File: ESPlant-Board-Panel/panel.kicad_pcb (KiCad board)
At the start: 4 copper layers, 142 x 116 mm, 342 parts, among them J1 Conn_01x05, U1 HC-TYPE-C-16P-01A-G, U13 ESP32-C6-MINI-1/U, U3 AHT20-F, U5 TPS61025DRCR, U6 Light sensor, U7 TS-1088-AR02016, U8 MK-12C02-G025

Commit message: Panel: Update production files
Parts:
- removed the BZ1 at (173.0, 57.5)
- removed the BZ1 at (251.0, 57.5)
- removed the BZ1 at (277.0, 57.5)
- removed the BZ1 at (199.0, 57.5)
- removed the BZ1 at (225.0, 57.5)
- removed the C1 at (220.5, 44.9)
- removed the C1 at (246.5, 44.9)
- removed the C1 at (194.5, 44.9)
- removed the C1 at (272.5, 44.9)
- removed the C1 at (168.5, 44.9)
- removed the C10 at (272.5, 51.2)
- removed the C10 at (194.5, 51.2)
- removed the C10 at (220.5, 51.2)
- removed the C10 at (246.5, 51.2)
- removed the C10 at (168.5, 51.2)
- removed the C2 at (168.5, 42.8)
- removed the C2 at (194.5, 42.8)
- removed the C2 at (272.5, 42.8)
- removed the C2 at (220.5, 42.8)
- removed the C2 at (246.5, 42.8)
- removed the C3 at (243.5, 32.2)
- removed the C3 at (191.5, 32.2)
- removed the C3 at (217.5, 32.2)
- removed the C3 at (165.5, 32.2)
- removed the C3 at (269.5, 32.2)
- removed the C4 at (199.0, 81.0)
- removed the C4 at (277.0, 81.0)
- removed the C4 at (173.0, 81.0)
- removed the C4 at (225.0, 81.0)
- removed the C4 at (251.0, 81.0)
- removed the C6 at (194.5, 49.7)
- removed the C6 at (246.5, 49.7)
- removed the C6 at (168.5, 49.7)
- removed the C6 at (272.5, 49.7)
- removed the C6 at (220.5, 49.7)
- removed the C7 at (255.3, 33.3)
- removed the C7 at (281.3, 33.3)
- removed the C7 at (229.3, 33.3)
- removed the C7 at (203.3, 33.3)
- removed the C7 at (177.3, 33.3)
- removed the C8 at (189.5, 22.4)
- removed the C8 at (215.5, 22.4)
- removed the C8 at (241.5, 22.4)
- removed the C8 at (267.5, 22.4)
- removed the C8 at (163.5, 22.4)
- removed the C9 at (240.5, 22.4)
- removed the C9 at (266.5, 22.4)
- removed the C9 at (162.5, 22.4)
- removed the C9 at (214.5, 22.4)
- removed the C9 at (188.5, 22.4)
- removed the D1 at (260.5, 35.3)
- removed the D1 at (208.5, 35.3)
- removed the D1 at (182.5, 35.3)
- removed the D1 at (286.5, 35.3)
- removed the D1 at (234.5, 35.3)
- removed the D2 at (219.3, 34.8)
- removed the D2 at (245.3, 34.8)
- removed the D2 at (193.3, 34.8)
- removed the D2 at (271.3, 34.8)
- removed the D2 at (167.3, 34.8)
- removed the D3 at (260.5, 33.0)
- removed the D3 at (286.5, 33.0)
- removed the D3 at (182.5, 33.0)
- removed the D3 at (234.5, 33.0)
- removed the D3 at (208.5, 33.0)
- removed the H1 at (286.4, 22.6)
- removed the H1 at (182.4, 22.6)
- removed the H1 at (260.4, 22.6)
- removed the H1 at (234.4, 22.6)
- removed the H1 at (208.4, 22.6)
- removed the H2 at (191.0, 60.0)
- removed the H2 at (243.0, 60.0)
- removed the H2 at (269.0, 60.0)
- removed the H2 at (165.0, 60.0)
- removed the H2 at (217.0, 60.0)
- removed the H3 at (259.0, 60.0)
- removed the H3 at (233.0, 60.0)
- removed the H3 at (285.0, 60.0)
- removed the H3 at (207.0, 60.0)
- removed the H3 at (181.0, 60.0)
- removed the J1 at (239.9, 42.4)
- removed the J1 at (187.9, 42.4)
- removed the J1 at (213.9, 42.4)
- removed the J1 at (265.9, 42.4)
- removed the J1 at (161.9, 42.4)
- removed the L1 at (198.5, 47.6)
- removed the L1 at (172.5, 47.6)
- removed the L1 at (250.5, 47.6)
- removed the L1 at (276.5, 47.6)
- removed the L1 at (224.5, 47.6)
- removed the R1 at (190.3, 45.3)
- removed the R1 at (164.3, 45.3)
- removed the R1 at (242.3, 45.3)
- removed the R1 at (216.3, 45.3)
- removed the R1 at (268.3, 45.3)
- removed the R10 at (283.4, 27.8)
- removed the R10 at (179.4, 27.8)
- removed the R10 at (231.4, 27.8)
- removed the R10 at (257.4, 27.8)
- removed the R10 at (205.4, 27.8)
- removed the R11 at (253.7, 43.0)
- removed the R11 at (175.7, 43.0)
- removed the R11 at (279.7, 43.0)
- removed the R11 at (227.7, 43.0)
- removed the R11 at (201.7, 43.0)
- removed the R12 at (253.7, 40.1)
- removed the R12 at (279.7, 40.1)
- removed the R12 at (175.7, 40.1)
- removed the R12 at (201.7, 40.1)
- removed the R12 at (227.7, 40.1)
- removed the R13 at (205.9, 35.3)
- removed the R13 at (231.9, 35.3)
- removed the R13 at (179.9, 35.3)
- removed the R13 at (257.9, 35.3)
- removed the R13 at (283.9, 35.3)
- removed the R14 at (179.9, 33.4)
- removed the R14 at (205.9, 33.4)
- removed the R14 at (231.9, 33.4)
- removed the R14 at (283.9, 33.4)
- removed the R14 at (257.9, 33.4)
- removed the R15 at (164.3, 46.3)
- removed the R15 at (216.3, 46.3)
- removed the R15 at (268.3, 46.3)
- removed the R15 at (242.3, 46.3)
- removed the R15 at (190.3, 46.3)
- removed the R16 at (190.8, 47.8)
- removed the R16 at (268.8, 47.8)
- removed the R16 at (216.8, 47.8)
- removed the R16 at (242.8, 47.8)
- removed the R16 at (164.8, 47.8)
- removed the R2 at (179.4, 25.9)
- removed the R2 at (283.4, 25.9)
- removed the R2 at (257.4, 25.9)
- removed the R2 at (205.4, 25.9)
- removed the R2 at (231.4, 25.9)
- removed the R3 at (203.3, 34.3)
- removed the R3 at (177.3, 34.3)
- removed the R3 at (229.3, 34.3)
- removed the R3 at (255.3, 34.3)
- removed the R3 at (281.3, 34.3)
- removed the R4 at (243.8, 37.9)
- removed the R4 at (165.8, 37.9)
- removed the R4 at (217.8, 37.9)
- removed the R4 at (191.8, 37.9)
- removed the R4 at (269.8, 37.9)
- removed the R5 at (173.6, 32.4)
- removed the R5 at (199.6, 32.4)
- removed the R5 at (251.6, 32.4)
- removed the R5 at (277.6, 32.4)
- removed the R5 at (225.6, 32.4)
- removed the R6 at (167.0, 36.9)
- removed the R6 at (193.0, 36.9)
- removed the R6 at (219.0, 36.9)
- removed the R6 at (245.0, 36.9)
- removed the R6 at (271.0, 36.9)
- removed the R7 at (227.1, 37.8)
- removed the R7 at (201.1, 37.8)
- removed the R7 at (175.1, 37.8)
- removed the R7 at (253.1, 37.8)
- removed the R7 at (279.1, 37.8)
- removed the R8 at (273.4, 32.6)
- removed the R8 at (195.4, 32.6)
- removed the R8 at (221.4, 32.6)
- removed the R8 at (247.4, 32.6)
- removed the R8 at (169.4, 32.6)
- removed the R9 at (215.0, 27.1)
- removed the R9 at (163.0, 27.1)
- removed the R9 at (267.0, 27.1)
- removed the R9 at (241.0, 27.1)
- removed the R9 at (189.0, 27.1)
- removed the U1 at (180.0, 41.6)
- removed the U1 at (232.0, 41.6)
- removed the U1 at (284.0, 41.6)
- removed the U1 at (206.0, 41.6)
- removed the U1 at (258.0, 41.6)
- removed the U13 at (274.9, 25.5)
- removed the U13 at (248.9, 25.5)
- removed the U13 at (196.9, 25.5)
- removed the U13 at (222.9, 25.5)
- removed the U13 at (170.9, 25.5)
- removed the U3 at (182.0, 28.1)
- removed the U3 at (208.0, 28.1)
- removed the U3 at (286.0, 28.1)
- removed the U3 at (234.0, 28.1)
- removed the U3 at (260.0, 28.1)
- removed the U5 at (246.5, 47.3)
- removed the U5 at (168.5, 47.3)
- removed the U5 at (272.5, 47.3)
- removed the U5 at (220.5, 47.3)
- removed the U5 at (194.5, 47.3)
- removed the U6 at (182.0, 30.9)
- removed the U6 at (234.0, 30.9)
- removed the U6 at (208.0, 30.9)
- removed the U6 at (260.0, 30.9)
- removed the U6 at (286.0, 30.9)
- removed the U7 at (242.7, 54.5)
- removed the U7 at (268.7, 54.5)
- removed the U7 at (164.7, 54.5)
- removed the U7 at (190.7, 54.5)
- removed the U7 at (216.7, 54.5)
- removed the U8 at (234.6, 51.5)
- removed the U8 at (286.6, 51.5)
- removed the U8 at (208.6, 51.5)
- removed the U8 at (182.6, 51.5)
- removed the U8 at (260.6, 51.5)
- removed the U9 at (277.0, 64.5)
- removed the U9 at (251.0, 64.5)
- removed the U9 at (173.0, 64.5)
- removed the U9 at (225.0, 64.5)
- removed the U9 at (199.0, 64.5)
- added BZ1: Buzzer, CustomFootprints:BUZ-SMD_4P-L8.5-W8.5-P8.50-BR, F.Cu at (173.0, 57.9)
- added BZ1: Buzzer, CustomFootprints:BUZ-SMD_4P-L8.5-W8.5-P8.50-BR, F.Cu at (277.0, 57.9)
- added BZ1: Buzzer, CustomFootprints:BUZ-SMD_4P-L8.5-W8.5-P8.50-BR, F.Cu at (199.0, 57.9)
- added BZ1: Buzzer, CustomFootprints:BUZ-SMD_4P-L8.5-W8.5-P8.50-BR, F.Cu at (225.0, 57.9)
- added BZ1: Buzzer, CustomFootprints:BUZ-SMD_4P-L8.5-W8.5-P8.50-BR, F.Cu at (251.0, 57.9)
- added C1: 2.2uF-Ceramic, Capacitor_SMD:C_0402_1005Metric, F.Cu at (258.3, 37.7)
- added C1: 2.2uF-Ceramic, Capacitor_SMD:C_0402_1005Metric, F.Cu at (180.3, 37.7)
- added C1: 2.2uF-Ceramic, Capacitor_SMD:C_0402_1005Metric, F.Cu at (284.3, 37.7)
- added C1: 2.2uF-Ceramic, Capacitor_SMD:C_0402_1005Metric, F.Cu at (206.3, 37.7)
- added C1: 2.2uF-Ceramic, Capacitor_SMD:C_0402_1005Metric, F.Cu at (232.3, 37.7)
- added C10: 10uF-Tantalum, CustomFootprints:CAP-SMD_L3.2-W1.6-RD-C7171, F.Cu at (200.0, 37.7)
- added C10: 10uF-Tantalum, CustomFootprints:CAP-SMD_L3.2-W1.6-RD-C7171, F.Cu at (278.0, 37.7)
- added C10: 10uF-Tantalum, CustomFootprints:CAP-SMD_L3.2-W1.6-RD-C7171, F.Cu at (252.0, 37.7)
- added C10: 10uF-Tantalum, CustomFootprints:CAP-SMD_L3.2-W1.6-RD-C7171, F.Cu at (226.0, 37.7)
- added C10: 10uF-Tantalum, CustomFootprints:CAP-SMD_L3.2-W1.6-RD-C7171, F.Cu at (174.0, 37.7)
- added C2: 100uF-Tantalum, CustomFootprints:CASE-B_3528, F.Cu at (234.4, 37.7)
- added C2: 100uF-Tantalum, CustomFootprints:CASE-B_3528, F.Cu at (208.4, 37.7)
- added C2: 100uF-Tantalum, CustomFootprints:CASE-B_3528, F.Cu at (182.4, 37.7)
- added C2: 100uF-Tantalum, CustomFootprints:CASE-B_3528, F.Cu at (260.4, 37.7)
- added C2: 100uF-Tantalum, CustomFootprints:CASE-B_3528, F.Cu at (286.4, 37.7)
- added C3: 10nF, Capacitor_SMD:C_0402_1005Metric, F.Cu at (219.1, 33.1)
- added C3: 10nF, Capacitor_SMD:C_0402_1005Metric, F.Cu at (271.1, 33.1)
- added C3: 10nF, Capacitor_SMD:C_0402_1005Metric, F.Cu at (167.1, 33.1)
- added C3: 10nF, Capacitor_SMD:C_0402_1005Metric, F.Cu at (245.1, 33.1)
- added C3: 10nF, Capacitor_SMD:C_0402_1005Metric, F.Cu at (193.1, 33.1)
- added C4: 7pF-27pF, A=2.75cm^2, CustomFootprints:Sensor-Tip, B.Cu at (251.0, 81.0)
- added C4: 7pF-27pF, A=2.75cm^2, CustomFootprints:Sensor-Tip, B.Cu at (173.0, 81.0)
- added C4: 7pF-27pF, A=2.75cm^2, CustomFootprints:Sensor-Tip, B.Cu at (277.0, 81.0)
- added C4: 7pF-27pF, A=2.75cm^2, CustomFootprints:Sensor-Tip, B.Cu at (199.0, 81.0)
- added C4: 7pF-27pF, A=2.75cm^2, CustomFootprints:Sensor-Tip, B.Cu at (225.0, 81.0)
- added C6: 100nF-Ceramic, Capacitor_SMD:C_0402_1005Metric, F.Cu at (253.5, 37.7)
- added C6: 100nF-Ceramic, Capacitor_SMD:C_0402_1005Metric, F.Cu at (279.5, 37.7)
- added C6: 100nF-Ceramic, Capacitor_SMD:C_0402_1005Metric, F.Cu at (201.5, 37.7)
- added C6: 100nF-Ceramic, Capacitor_SMD:C_0402_1005Metric, F.Cu at (175.5, 37.7)
- added C6: 100nF-Ceramic, Capacitor_SMD:C_0402_1005Metric, F.Cu at (227.5, 37.7)
- added C7: 10uF, Capacitor_SMD:C_0402_1005Metric, F.Cu at (163.5, 26.9)
- added C7: 10uF, Capacitor_SMD:C_0402_1005Metric, F.Cu at (241.5, 26.9)
- added C7: 10uF, Capacitor_SMD:C_0402_1005Metric, F.Cu at (189.5, 26.9)
- added C7: 10uF, Capacitor_SMD:C_0402_1005Metric, F.Cu at (215.5, 26.9)
- added C7: 10uF, Capacitor_SMD:C_0402_1005Metric, F.Cu at (267.5, 26.9)
- added C8: 10nF, Capacitor_SMD:C_0402_1005Metric, F.Cu at (242.8, 22.4)
- added C8: 10nF, Capacitor_SMD:C_0402_1005Metric, F.Cu at (164.8, 22.4)
- added C8: 10nF, Capacitor_SMD:C_0402_1005Metric, F.Cu at (190.8, 22.4)
- added C8: 10nF, Capacitor_SMD:C_0402_1005Metric, F.Cu at (216.8, 22.4)
- added C8: 10nF, Capacitor_SMD:C_0402_1005Metric, F.Cu at (268.8, 22.4)
- added C9: 10uF, Capacitor_SMD:C_0402_1005Metric, F.Cu at (215.8, 22.4)
- added C9: 10uF, Capacitor_SMD:C_0402_1005Metric, F.Cu at (267.8, 22.4)
- added C9: 10uF, Capacitor_SMD:C_0402_1005Metric, F.Cu at (241.8, 22.4)
- added C9: 10uF, Capacitor_SMD:C_0402_1005Metric, F.Cu at (163.8, 22.4)
- added C9: 10uF, Capacitor_SMD:C_0402_1005Metric, F.Cu at (189.8, 22.4)
- added D1: GREEN, CustomFootprints:LED0805-R-RD, F.Cu at (269.7, 40.5)
- added D1: GREEN, CustomFootprints:LED0805-R-RD, F.Cu at (191.7, 40.5)
- added D1: GREEN, CustomFootprints:LED0805-R-RD, F.Cu at (217.7, 40.5)
- added D1: GREEN, CustomFootprints:LED0805-R-RD, F.Cu at (243.7, 40.5)
- added D1: GREEN, CustomFootprints:LED0805-R-RD, F.Cu at (165.7, 40.5)
- added D2: Switching-Diode, CustomFootprints:SOD-123F_L2.7-W1.6-LS3.8-RD, F.Cu at (194.8, 34.7)
- added D2: Switching-Diode, CustomFootprints:SOD-123F_L2.7-W1.6-LS3.8-RD, F.Cu at (246.8, 34.7)
- added D2: Switching-Diode, CustomFootprints:SOD-123F_L2.7-W1.6-LS3.8-RD, F.Cu at (168.8, 34.7)
- added D2: Switching-Diode, CustomFootprints:SOD-123F_L2.7-W1.6-LS3.8-RD, F.Cu at (272.8, 34.7)
- added D2: Switching-Diode, CustomFootprints:SOD-123F_L2.7-W1.6-LS3.8-RD, F.Cu at (220.8, 34.7)
- added D3: RED, CustomFootprints:LED0805-R-RD, F.Cu at (241.7, 40.5)
- added D3: RED, CustomFootprints:LED0805-R-RD, F.Cu at (189.7, 40.5)
- added D3: RED, CustomFootprints:LED0805-R-RD, F.Cu at (215.7, 40.5)
- added D3: RED, CustomFootprints:LED0805-R-RD, F.Cu at (267.7, 40.5)
- added D3: RED, CustomFootprints:LED0805-R-RD, F.Cu at (163.7, 40.5)
- added H1: MountingHole, MountingHole:MountingHole_3.2mm_M3, F.Cu at (234.4, 22.6)
- added H1: MountingHole, MountingHole:MountingHole_3.2mm_M3, F.Cu at (286.4, 22.6)
- added H1: MountingHole, MountingHole:MountingHole_3.2mm_M3, F.Cu at (260.4, 22.6)
- added H1: MountingHole, MountingHole:MountingHole_3.2mm_M3, F.Cu at (208.4, 22.6)
- added H1: MountingHole, MountingHole:MountingHole_3.2mm_M3, F.Cu at (182.4, 22.6)
- added H2: MountingHole, MountingHole:MountingHole_3.2mm_M3, F.Cu at (241.6, 60.7)
- added H2: MountingHole, MountingHole:MountingHole_3.2mm_M3, F.Cu at (267.6, 60.7)
- added H2: MountingHole, MountingHole:MountingHole_3.2mm_M3, F.Cu at (189.6, 60.7)
- added H2: MountingHole, MountingHole:MountingHole_3.2mm_M3, F.Cu at (215.6, 60.7)
- added H2: MountingHole, MountingHole:MountingHole_3.2mm_M3, F.Cu at (163.6, 60.7)
- added H3: MountingHole, MountingHole:MountingHole_3.2mm_M3, F.Cu at (234.4, 60.7)
- added H3: MountingHole, MountingHole:MountingHole_3.2mm_M3, F.Cu at (182.4, 60.7)
- added H3: MountingHole, MountingHole:MountingHole_3.2mm_M3, F.Cu at (208.4, 60.7)
- added H3: MountingHole, MountingHole:MountingHole_3.2mm_M3, F.Cu at (260.4, 60.7)
- added H3: MountingHole, MountingHole:MountingHole_3.2mm_M3, F.Cu at (286.4, 60.7)
- added J1: Conn_01x05, CustomFootprints:PinHeader_1x05_P2.54mm_Vertical_SMD, B.Cu at (240.0, 35.8)
- added J1: Conn_01x05, CustomFootprints:PinHeader_1x05_P2.54mm_Vertical_SMD, B.Cu at (188.0, 35.8)
- added J1: Conn_01x05, CustomFootprints:PinHeader_1x05_P2.54mm_Vertical_SMD, B.Cu at (162.0, 35.8)
- added J1: Conn_01x05, CustomFootprints:PinHeader_1x05_P2.54mm_Vertical_SMD, B.Cu at (266.0, 35.8)
- added J1: Conn_01x05, CustomFootprints:PinHeader_1x05_P2.54mm_Vertical_SMD, B.Cu at (214.0, 35.8)
- added L1: 6.8uH, CustomFootprints:IND-SMD_L3.5-W3.0, F.Cu at (281.6, 41.7)
- added L1: 6.8uH, CustomFootprints:IND-SMD_L3.5-W3.0, F.Cu at (255.6, 41.7)
- added L1: 6.8uH, CustomFootprints:IND-SMD_L3.5-W3.0, F.Cu at (177.6, 41.7)
- added L1: 6.8uH, CustomFootprints:IND-SMD_L3.5-W3.0, F.Cu at (229.6, 41.7)
- added L1: 6.8uH, CustomFootprints:IND-SMD_L3.5-W3.0, F.Cu at (203.6, 41.7)
- added R1: 100k, Resistor_SMD:R_0402_1005Metric, F.Cu at (205.9, 33.5)
- added R1: 100k, Resistor_SMD:R_0402_1005Metric, F.Cu at (257.9, 33.5)
- added R1: 100k, Resistor_SMD:R_0402_1005Metric, F.Cu at (179.9, 33.5)
- added R1: 100k, Resistor_SMD:R_0402_1005Metric, F.Cu at (231.9, 33.5)
- added R1: 100k, Resistor_SMD:R_0402_1005Metric, F.Cu at (283.9, 33.5)
- added R10: 5k1, Resistor_SMD:R_0402_1005Metric, F.Cu at (179.4, 27.9)
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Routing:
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- added copper zone on F.Cu, net Board_0-PWR_VIN
- added copper zone on F.Cu, net Board_1-PWR_VIN
- added copper zone on F.Cu, net Board_2-PWR_VIN
- added copper zone on F.Cu, net Board_3-PWR_VIN
- added copper zone on F.Cu, net Board_4-PWR_VIN
- removed copper zone on F.Cu, net Board_0-VCC
- removed copper zone on F.Cu, net Board_1-VCC
- removed copper zone on F.Cu, net Board_2-VCC
- removed copper zone on F.Cu, net Board_3-VCC
- removed copper zone on F.Cu, net Board_4-VCC
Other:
- outline, holes or cut-outs redrawn
- board text added: "Reset"
- board text added: "USB〡BAT"

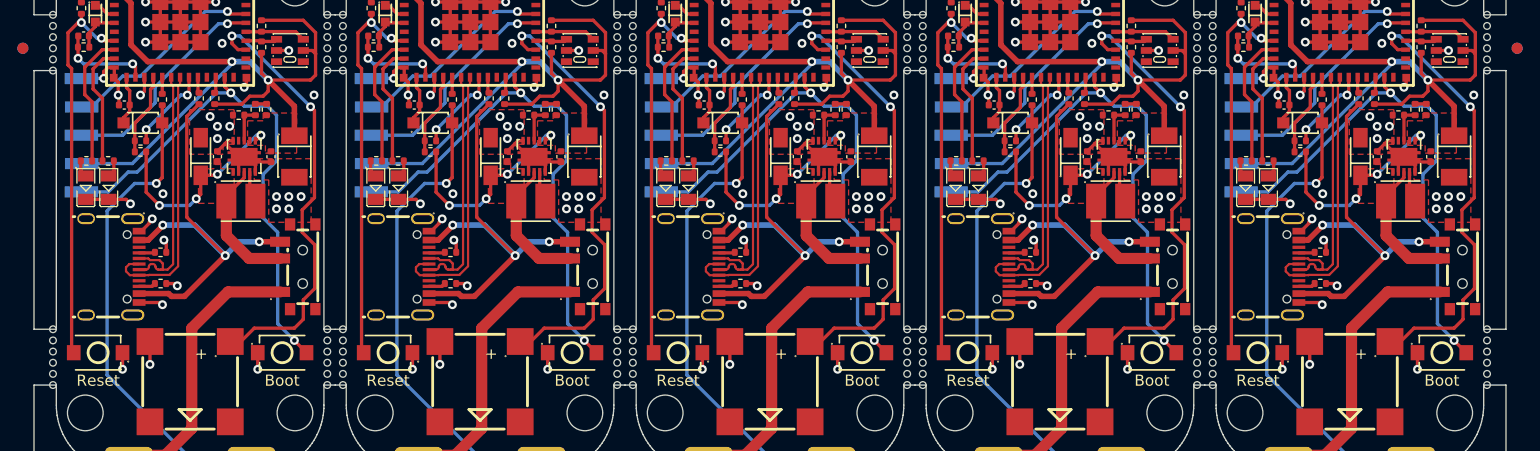
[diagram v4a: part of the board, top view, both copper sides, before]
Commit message: Board: Add debouncing caps to buttons
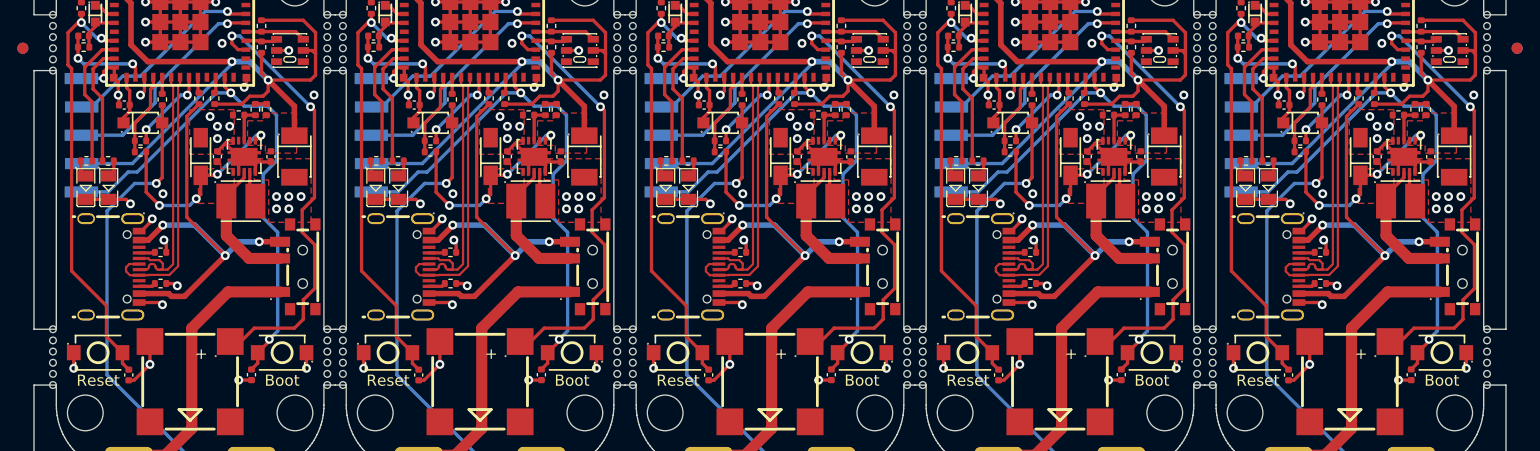
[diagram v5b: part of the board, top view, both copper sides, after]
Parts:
- added C11: 100nF-Ceramic, Capacitor_SMD:C_0402_1005Metric, F.Cu at (219.5, 57.3)
- added C11: 100nF-Ceramic, Capacitor_SMD:C_0402_1005Metric, F.Cu at (245.5, 57.3)
- added C11: 100nF-Ceramic, Capacitor_SMD:C_0402_1005Metric, F.Cu at (167.5, 57.3)
- added C11: 100nF-Ceramic, Capacitor_SMD:C_0402_1005Metric, F.Cu at (193.5, 57.3)
- added C11: 100nF-Ceramic, Capacitor_SMD:C_0402_1005Metric, F.Cu at (271.5, 57.3)
- added C5: 100nF-Ceramic, Capacitor_SMD:C_0402_1005Metric, F.Cu at (256.5, 57.3)
- added C5: 100nF-Ceramic, Capacitor_SMD:C_0402_1005Metric, F.Cu at (230.5, 57.3)
- added C5: 100nF-Ceramic, Capacitor_SMD:C_0402_1005Metric, F.Cu at (282.5, 57.3)
- added C5: 100nF-Ceramic, Capacitor_SMD:C_0402_1005Metric, F.Cu at (204.5, 57.3)
- added C5: 100nF-Ceramic, Capacitor_SMD:C_0402_1005Metric, F.Cu at (178.5, 57.3)
- turned U4 to 0 degrees (x5)
- turned U7 to 180 degrees (x5)
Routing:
- net Board_1-GND: track 214.8 -> 218.5 mm, vias 47 -> 48
- net Board_0-GND: track 214.8 -> 218.5 mm, vias 47 -> 48
- net Board_2-GND: track 214.8 -> 218.5 mm, vias 47 -> 48
- net Board_4-GND: track 214.8 -> 218.5 mm, vias 47 -> 48
- net Board_3-GND: track 214.8 -> 218.5 mm, vias 47 -> 48
- net Board_2-EN: track 34.9 -> 38.5 mm
- net Board_4-EN: track 34.9 -> 38.5 mm
- net Board_3-EN: track 34.9 -> 38.5 mm
- net Board_1-EN: track 34.9 -> 38.5 mm
- net Board_0-EN: track 34.9 -> 38.5 mm
- net Board_3-IO9: track 47.0 -> 48.4 mm
- net Board_4-IO9: track 47.0 -> 48.4 mm
- net Board_2-IO9: track 47.0 -> 48.4 mm
- net Board_0-IO9: track 47.0 -> 48.4 mm
- net Board_1-IO9: track 47.0 -> 48.4 mm

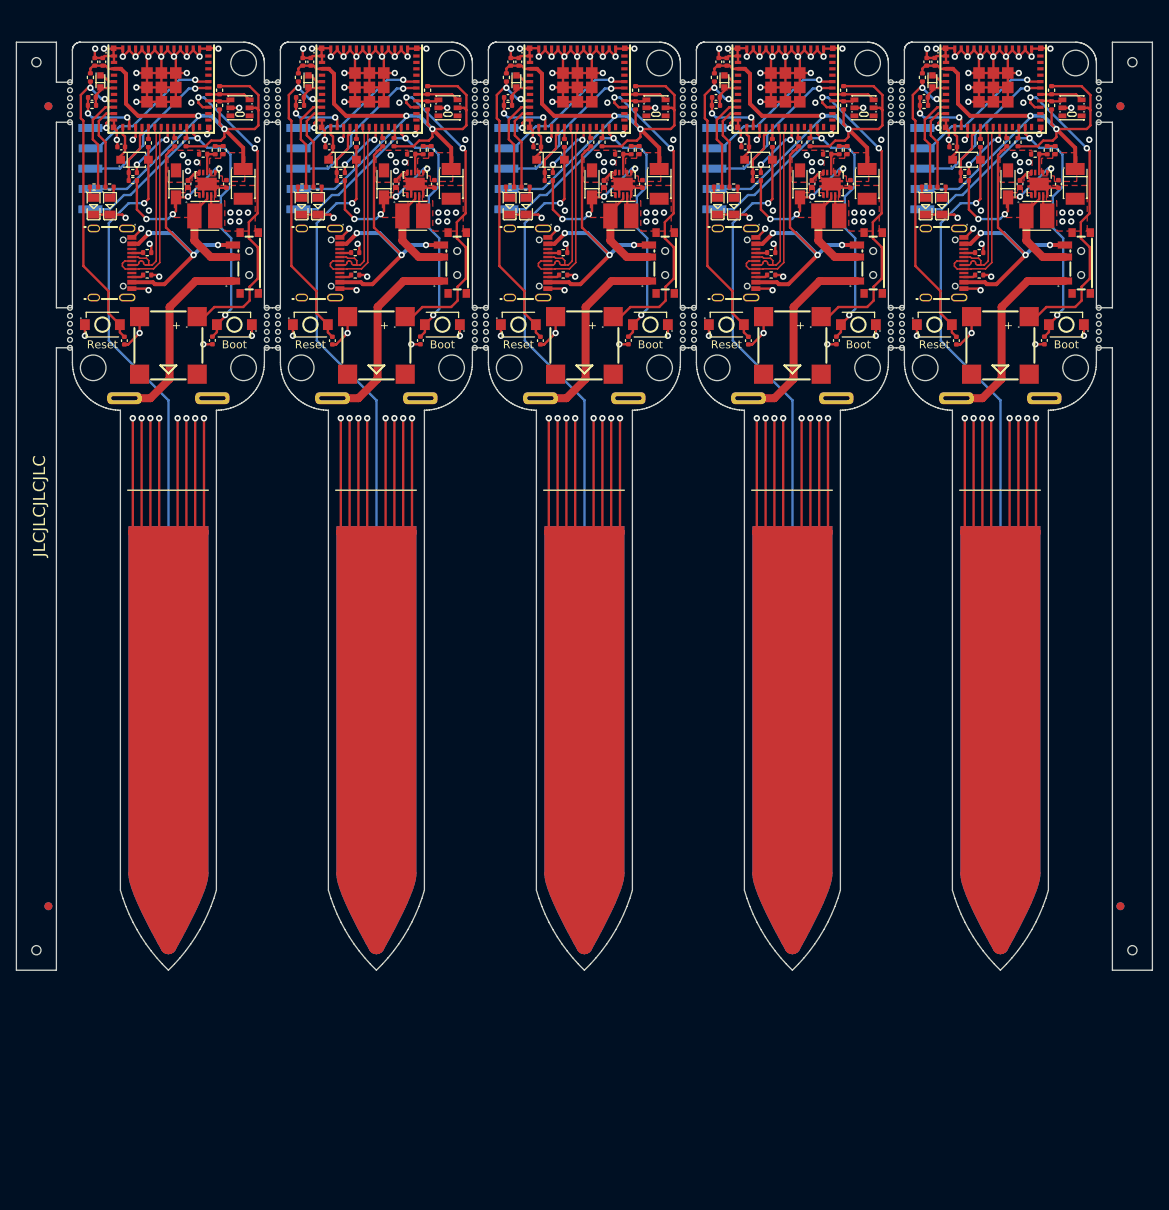
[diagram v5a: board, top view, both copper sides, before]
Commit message: Panel: 2 columns
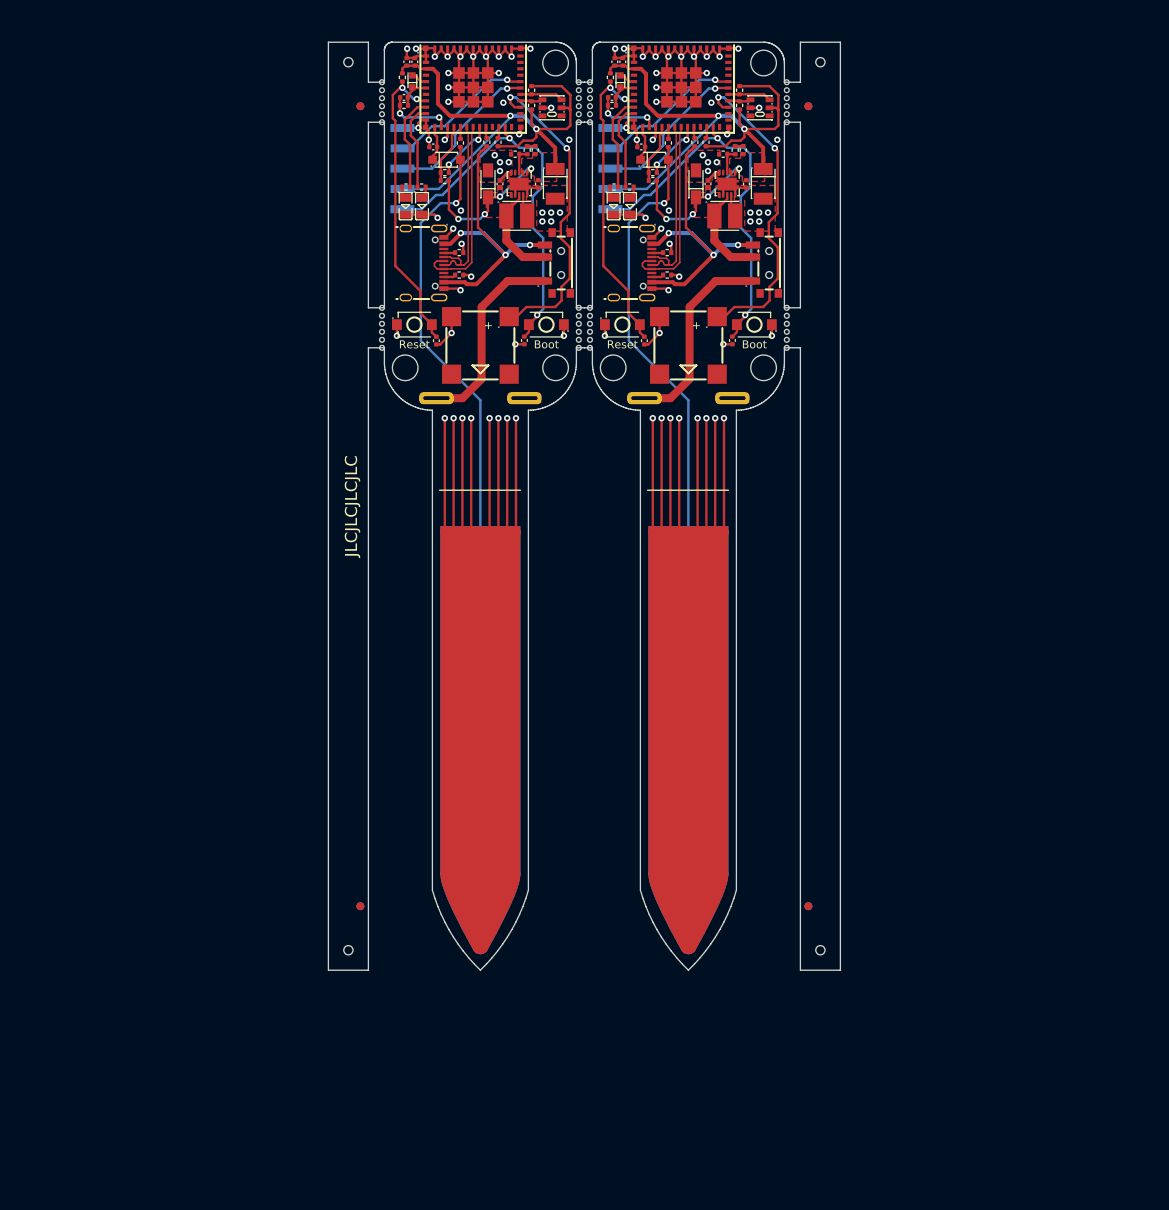
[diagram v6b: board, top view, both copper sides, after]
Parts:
- removed the BZ1 at (199.0, 57.9)
- removed the BZ1 at (251.0, 57.9)
- removed the BZ1 at (277.0, 57.9)
- removed the BZ1 at (225.0, 57.9)
- removed the BZ1 at (173.0, 57.9)
- removed the C1 at (232.3, 37.7)
- removed the C1 at (180.3, 37.7)
- removed the C1 at (258.3, 37.7)
- removed the C1 at (284.3, 37.7)
- removed the C1 at (206.3, 37.7)
- removed the C10 at (252.0, 37.7)
- removed the C10 at (200.0, 37.7)
- removed the C10 at (226.0, 37.7)
- removed the C10 at (278.0, 37.7)
- removed the C10 at (174.0, 37.7)
- removed the C11 at (219.5, 57.3)
- removed the C11 at (245.5, 57.3)
- removed the C11 at (167.5, 57.3)
- removed the C11 at (193.5, 57.3)
- removed the C11 at (271.5, 57.3)
- removed the C2 at (260.4, 37.7)
- removed the C2 at (234.4, 37.7)
- removed the C2 at (182.4, 37.7)
- removed the C2 at (286.4, 37.7)
- removed the C2 at (208.4, 37.7)
- removed the C3 at (245.1, 33.1)
- removed the C3 at (167.1, 33.1)
- removed the C3 at (219.1, 33.1)
- removed the C3 at (271.1, 33.1)
- removed the C3 at (193.1, 33.1)
- removed the C4 at (199.0, 81.0)
- removed the C4 at (277.0, 81.0)
- removed the C4 at (251.0, 81.0)
- removed the C4 at (173.0, 81.0)
- removed the C4 at (225.0, 81.0)
- removed the C5 at (256.5, 57.3)
- removed the C5 at (230.5, 57.3)
- removed the C5 at (282.5, 57.3)
- removed the C5 at (204.5, 57.3)
- removed the C5 at (178.5, 57.3)
- removed the C6 at (279.5, 37.7)
- removed the C6 at (253.5, 37.7)
- removed the C6 at (175.5, 37.7)
- removed the C6 at (201.5, 37.7)
- removed the C6 at (227.5, 37.7)
- removed the C7 at (163.5, 26.9)
- removed the C7 at (241.5, 26.9)
- removed the C7 at (267.5, 26.9)
- removed the C7 at (215.5, 26.9)
- removed the C7 at (189.5, 26.9)
- removed the C8 at (216.8, 22.4)
- removed the C8 at (190.8, 22.4)
- removed the C8 at (242.8, 22.4)
- removed the C8 at (268.8, 22.4)
- removed the C8 at (164.8, 22.4)
- removed the C9 at (241.8, 22.4)
- removed the C9 at (215.8, 22.4)
- removed the C9 at (189.8, 22.4)
- removed the C9 at (267.8, 22.4)
- removed the C9 at (163.8, 22.4)
- removed the D1 at (217.7, 40.5)
- removed the D1 at (243.7, 40.5)
- removed the D1 at (269.7, 40.5)
- removed the D1 at (191.7, 40.5)
- removed the D1 at (165.7, 40.5)
- removed the D2 at (246.8, 34.7)
- removed the D2 at (220.8, 34.7)
- removed the D2 at (194.8, 34.7)
- removed the D2 at (168.8, 34.7)
- removed the D2 at (272.8, 34.7)
- removed the D3 at (189.7, 40.5)
- removed the D3 at (163.7, 40.5)
- removed the D3 at (215.7, 40.5)
- removed the D3 at (267.7, 40.5)
- removed the D3 at (241.7, 40.5)
- removed the H1 at (182.4, 22.6)
- removed the H1 at (286.4, 22.6)
- removed the H1 at (208.4, 22.6)
- removed the H1 at (260.4, 22.6)
- removed the H1 at (234.4, 22.6)
- removed the H2 at (215.6, 60.7)
- removed the H2 at (189.6, 60.7)
- removed the H2 at (267.6, 60.7)
- removed the H2 at (163.6, 60.7)
- removed the H2 at (241.6, 60.7)
- removed the H3 at (234.4, 60.7)
- removed the H3 at (182.4, 60.7)
- removed the H3 at (260.4, 60.7)
- removed the H3 at (286.4, 60.7)
- removed the H3 at (208.4, 60.7)
- removed the J1 at (188.0, 35.8)
- removed the J1 at (240.0, 35.8)
- removed the J1 at (214.0, 35.8)
- removed the J1 at (266.0, 35.8)
- removed the J1 at (162.0, 35.8)
- removed KiKit_MB_10_1, KiKit_MB_10_2, KiKit_MB_10_3, KiKit_MB_10_4, KiKit_MB_10_5, KiKit_MB_10_6, KiKit_MB_11_1, KiKit_MB_11_2, KiKit_MB_11_3, KiKit_MB_11_4, KiKit_MB_11_5, KiKit_MB_11_6, KiKit_MB_12_1, KiKit_MB_12_2, KiKit_MB_12_3, KiKit_MB_12_4, KiKit_MB_12_5, KiKit_MB_12_6, KiKit_MB_13_1, KiKit_MB_13_2, KiKit_MB_13_3, KiKit_MB_13_4, KiKit_MB_13_5, KiKit_MB_13_6, KiKit_MB_14_1, KiKit_MB_14_2, KiKit_MB_14_3, KiKit_MB_14_4, KiKit_MB_14_5, KiKit_MB_14_6, KiKit_MB_15_1, KiKit_MB_15_2, KiKit_MB_15_3, KiKit_MB_15_4, KiKit_MB_15_5, KiKit_MB_15_6, KiKit_MB_16_1, KiKit_MB_16_2, KiKit_MB_16_3, KiKit_MB_16_4, KiKit_MB_16_5, KiKit_MB_16_6, KiKit_MB_17_1, KiKit_MB_17_2, KiKit_MB_17_3, KiKit_MB_17_4, KiKit_MB_17_5, KiKit_MB_17_6, KiKit_MB_18_1, KiKit_MB_18_2, KiKit_MB_18_3, KiKit_MB_18_4, KiKit_MB_18_5, KiKit_MB_18_6, KiKit_MB_19_1, KiKit_MB_19_2, KiKit_MB_19_3, KiKit_MB_19_4, KiKit_MB_19_5, KiKit_MB_19_6, KiKit_MB_20_1, KiKit_MB_20_2, KiKit_MB_20_3, KiKit_MB_20_4, KiKit_MB_20_5, KiKit_MB_20_6, KiKit_MB_9_1, KiKit_MB_9_2, KiKit_MB_9_3, KiKit_MB_9_4, KiKit_MB_9_5, KiKit_MB_9_6: NPTH, NPTH
- removed the L1 at (229.6, 41.7)
- removed the L1 at (281.6, 41.7)
- removed the L1 at (255.6, 41.7)
- removed the L1 at (177.6, 41.7)
- removed the L1 at (203.6, 41.7)
- removed the R1 at (231.9, 33.5)
- removed the R1 at (179.9, 33.5)
- removed the R1 at (205.9, 33.5)
- removed the R1 at (283.9, 33.5)
- removed the R1 at (257.9, 33.5)
- removed the R10 at (231.4, 27.9)
- removed the R10 at (283.4, 27.9)
- removed the R10 at (205.4, 27.9)
- removed the R10 at (257.4, 27.9)
- removed the R10 at (179.4, 27.9)
- removed the R11 at (248.4, 46.3)
- removed the R11 at (274.4, 46.3)
- removed the R11 at (196.4, 46.3)
- removed the R11 at (222.4, 46.3)
- removed the R11 at (170.4, 46.3)
- removed the R12 at (196.4, 49.1)
- removed the R12 at (170.4, 49.1)
- removed the R12 at (248.4, 49.1)
- removed the R12 at (222.4, 49.1)
- removed the R12 at (274.4, 49.1)
- removed the R13 at (217.7, 38.1)
- removed the R13 at (165.7, 38.1)
- removed the R13 at (191.7, 38.1)
- removed the R13 at (269.7, 38.1)
- removed the R13 at (243.7, 38.1)
- removed the R14 at (215.7, 38.1)
- removed the R14 at (163.7, 38.1)
- removed the R14 at (267.7, 38.1)
- removed the R14 at (189.7, 38.1)
- removed the R14 at (241.7, 38.1)
- removed the R15 at (282.9, 33.5)
- removed the R15 at (230.9, 33.5)
- removed the R15 at (256.9, 33.5)
- removed the R15 at (178.9, 33.5)
- removed the R15 at (204.9, 33.5)
- removed the R16 at (281.4, 34.0)
- removed the R16 at (203.4, 34.0)
- removed the R16 at (255.4, 34.0)
- removed the R16 at (177.4, 34.0)
- removed the R16 at (229.4, 34.0)
- removed the R2 at (283.4, 26.0)
- removed the R2 at (257.4, 26.0)
- removed the R2 at (205.4, 26.0)
- removed the R2 at (231.4, 26.0)
- removed the R2 at (179.4, 26.0)
- removed the R3 at (241.5, 27.9)
- removed the R3 at (215.5, 27.9)
- removed the R3 at (163.5, 27.9)
- removed the R3 at (267.5, 27.9)
- removed the R3 at (189.5, 27.9)
- removed the R4 at (194.6, 37.3)
- removed the R4 at (272.6, 37.3)
- removed the R4 at (220.6, 37.3)
- removed the R4 at (246.6, 37.3)
- removed the R4 at (168.6, 37.3)
- removed the R5 at (201.2, 32.5)
- removed the R5 at (227.2, 32.5)
- removed the R5 at (253.2, 32.5)
- removed the R5 at (175.2, 32.5)
- removed the R5 at (279.2, 32.5)
- removed the R6 at (272.6, 36.3)
- removed the R6 at (194.6, 36.3)
- removed the R6 at (220.6, 36.3)
- removed the R6 at (246.6, 36.3)
- removed the R6 at (168.6, 36.3)
- removed the R7 at (251.8, 32.5)
- removed the R7 at (199.8, 32.5)
- removed the R7 at (225.8, 32.5)
- removed the R7 at (173.8, 32.5)
- removed the R7 at (277.8, 32.5)
- removed the R8 at (196.5, 32.6)
- removed the R8 at (274.5, 32.6)
- removed the R8 at (248.5, 32.6)
- removed the R8 at (222.5, 32.6)
- removed the R8 at (170.5, 32.6)
- removed the R9 at (241.3, 24.4)
- removed the R9 at (267.3, 24.4)
- removed the R9 at (163.3, 24.4)
- removed the R9 at (215.3, 24.4)
- removed the R9 at (189.3, 24.4)
- removed the U1 at (166.1, 47.6)
- removed the U1 at (244.1, 47.6)
- removed the U1 at (218.1, 47.6)
- removed the U1 at (192.1, 47.6)
- removed the U1 at (270.1, 47.6)
- removed the U13 at (198.1, 25.7)
- removed the U13 at (172.1, 25.7)
- removed the U13 at (250.1, 25.7)
- removed the U13 at (224.1, 25.7)
- removed the U13 at (276.1, 25.7)
- removed the U3 at (208.0, 28.2)
- removed the U3 at (286.0, 28.2)
- removed the U3 at (260.0, 28.2)
- removed the U3 at (234.0, 28.2)
- removed the U3 at (182.0, 28.2)
- removed the U4 at (216.8, 55.3)
- removed the U4 at (190.8, 55.3)
- removed the U4 at (164.8, 55.3)
- removed the U4 at (242.8, 55.3)
- removed the U4 at (268.8, 55.3)
- removed the U5 at (229.9, 37.7)
- removed the U5 at (255.9, 37.7)
- removed the U5 at (177.9, 37.7)
- removed the U5 at (281.9, 37.7)
- removed the U5 at (203.9, 37.7)
- removed the U6 at (190.5, 24.9)
- removed the U6 at (164.5, 24.9)
- removed the U6 at (242.5, 24.9)
- removed the U6 at (216.5, 24.9)
- removed the U6 at (268.5, 24.9)
- removed the U7 at (233.3, 55.3)
- removed the U7 at (207.3, 55.3)
- removed the U7 at (285.3, 55.3)
- removed the U7 at (181.3, 55.3)
- removed the U7 at (259.3, 55.3)
- removed the U8 at (286.7, 47.6)
- removed the U8 at (260.7, 47.6)
- removed the U8 at (208.7, 47.6)
- removed the U8 at (182.7, 47.6)
- removed the U8 at (234.7, 47.6)
- removed the U9 at (225.0, 64.5)
- removed the U9 at (251.0, 64.5)
- removed the U9 at (199.0, 64.5)
- removed the U9 at (277.0, 64.5)
- removed the U9 at (173.0, 64.5)
- added BZ1: Buzzer, CustomFootprints:BUZ-SMD_4P-L8.5-W8.5-P8.50-BR, F.Cu at (212.0, 57.9)
- added BZ1: Buzzer, CustomFootprints:BUZ-SMD_4P-L8.5-W8.5-P8.50-BR, F.Cu at (238.0, 57.9)
- added C1: 2.2uF-Ceramic, Capacitor_SMD:C_0402_1005Metric, F.Cu at (245.3, 37.7)
- added C1: 2.2uF-Ceramic, Capacitor_SMD:C_0402_1005Metric, F.Cu at (219.3, 37.7)
- added C10: 10uF-Tantalum, CustomFootprints:CAP-SMD_L3.2-W1.6-RD-C7171, F.Cu at (239.0, 37.7)
- added C10: 10uF-Tantalum, CustomFootprints:CAP-SMD_L3.2-W1.6-RD-C7171, F.Cu at (213.0, 37.7)
- added C11: 100nF-Ceramic, Capacitor_SMD:C_0402_1005Metric, F.Cu at (232.5, 57.3)
- added C11: 100nF-Ceramic, Capacitor_SMD:C_0402_1005Metric, F.Cu at (206.5, 57.3)
- added C2: 100uF-Tantalum, CustomFootprints:CASE-B_3528, F.Cu at (221.4, 37.7)
- added C2: 100uF-Tantalum, CustomFootprints:CASE-B_3528, F.Cu at (247.4, 37.7)
- added C3: 10nF, Capacitor_SMD:C_0402_1005Metric, F.Cu at (232.1, 33.1)
- added C3: 10nF, Capacitor_SMD:C_0402_1005Metric, F.Cu at (206.1, 33.1)
- added C4: 7pF-27pF, A=2.75cm^2, CustomFootprints:Sensor-Tip, B.Cu at (238.0, 81.0)
- added C4: 7pF-27pF, A=2.75cm^2, CustomFootprints:Sensor-Tip, B.Cu at (212.0, 81.0)
- added C5: 100nF-Ceramic, Capacitor_SMD:C_0402_1005Metric, F.Cu at (243.5, 57.3)
- added C5: 100nF-Ceramic, Capacitor_SMD:C_0402_1005Metric, F.Cu at (217.5, 57.3)
- added C6: 100nF-Ceramic, Capacitor_SMD:C_0402_1005Metric, F.Cu at (214.5, 37.7)
- added C6: 100nF-Ceramic, Capacitor_SMD:C_0402_1005Metric, F.Cu at (240.5, 37.7)
- added C7: 10uF, Capacitor_SMD:C_0402_1005Metric, F.Cu at (202.5, 26.9)
- added C7: 10uF, Capacitor_SMD:C_0402_1005Metric, F.Cu at (228.5, 26.9)
- added C8: 10nF, Capacitor_SMD:C_0402_1005Metric, F.Cu at (203.8, 22.4)
- added C8: 10nF, Capacitor_SMD:C_0402_1005Metric, F.Cu at (229.8, 22.4)
- added C9: 10uF, Capacitor_SMD:C_0402_1005Metric, F.Cu at (228.8, 22.4)
- added C9: 10uF, Capacitor_SMD:C_0402_1005Metric, F.Cu at (202.8, 22.4)
- added D1: GREEN, CustomFootprints:LED0805-R-RD, F.Cu at (204.7, 40.5)
- added D1: GREEN, CustomFootprints:LED0805-R-RD, F.Cu at (230.7, 40.5)
- added D2: Switching-Diode, CustomFootprints:SOD-123F_L2.7-W1.6-LS3.8-RD, F.Cu at (207.8, 34.7)
- added D2: Switching-Diode, CustomFootprints:SOD-123F_L2.7-W1.6-LS3.8-RD, F.Cu at (233.8, 34.7)
- added D3: RED, CustomFootprints:LED0805-R-RD, F.Cu at (228.7, 40.5)
- added D3: RED, CustomFootprints:LED0805-R-RD, F.Cu at (202.7, 40.5)
- added H1: MountingHole, MountingHole:MountingHole_3.2mm_M3, F.Cu at (221.4, 22.6)
- added H1: MountingHole, MountingHole:MountingHole_3.2mm_M3, F.Cu at (247.4, 22.6)
- added H2: MountingHole, MountingHole:MountingHole_3.2mm_M3, F.Cu at (228.6, 60.7)
- added H2: MountingHole, MountingHole:MountingHole_3.2mm_M3, F.Cu at (202.6, 60.7)
- added H3: MountingHole, MountingHole:MountingHole_3.2mm_M3, F.Cu at (247.4, 60.7)
- added H3: MountingHole, MountingHole:MountingHole_3.2mm_M3, F.Cu at (221.4, 60.7)
- added J1: Conn_01x05, CustomFootprints:PinHeader_1x05_P2.54mm_Vertical_SMD, B.Cu at (227.0, 35.8)
- added J1: Conn_01x05, CustomFootprints:PinHeader_1x05_P2.54mm_Vertical_SMD, B.Cu at (201.0, 35.8)
- added L1: 6.8uH, CustomFootprints:IND-SMD_L3.5-W3.0, F.Cu at (216.6, 41.7)
- added L1: 6.8uH, CustomFootprints:IND-SMD_L3.5-W3.0, F.Cu at (242.6, 41.7)
- added R1: 100k, Resistor_SMD:R_0402_1005Metric, F.Cu at (244.9, 33.5)
- added R1: 100k, Resistor_SMD:R_0402_1005Metric, F.Cu at (218.9, 33.5)
- added R10: 5k1, Resistor_SMD:R_0402_1005Metric, F.Cu at (244.4, 27.9)
- added R10: 5k1, Resistor_SMD:R_0402_1005Metric, F.Cu at (218.4, 27.9)
- added R11: 5k1, Resistor_SMD:R_0402_1005Metric, F.Cu at (209.4, 46.3)
- added R11: 5k1, Resistor_SMD:R_0402_1005Metric, F.Cu at (235.4, 46.3)
- added R12: 5k1, Resistor_SMD:R_0402_1005Metric, F.Cu at (235.4, 49.1)
- added R12: 5k1, Resistor_SMD:R_0402_1005Metric, F.Cu at (209.4, 49.1)
- added R13: 120, Resistor_SMD:R_0402_1005Metric, F.Cu at (230.7, 38.1)
- added R13: 120, Resistor_SMD:R_0402_1005Metric, F.Cu at (204.7, 38.1)
- added R14: 120, Resistor_SMD:R_0402_1005Metric, F.Cu at (202.7, 38.1)
- added R14: 120, Resistor_SMD:R_0402_1005Metric, F.Cu at (228.7, 38.1)
- added R15: 1M, Resistor_SMD:R_0402_1005Metric, F.Cu at (243.9, 33.5)
- added R15: 1M, Resistor_SMD:R_0402_1005Metric, F.Cu at (217.9, 33.5)
- added R16: 200k, Resistor_SMD:R_0402_1005Metric, F.Cu at (216.4, 34.0)
- added R16: 200k, Resistor_SMD:R_0402_1005Metric, F.Cu at (242.4, 34.0)
- added R2: 5k1, Resistor_SMD:R_0402_1005Metric, F.Cu at (218.4, 26.0)
- added R2: 5k1, Resistor_SMD:R_0402_1005Metric, F.Cu at (244.4, 26.0)
- added R3: 47k, Resistor_SMD:R_0402_1005Metric, F.Cu at (202.5, 27.9)
- added R3: 47k, Resistor_SMD:R_0402_1005Metric, F.Cu at (228.5, 27.9)
- added R4: 5k1, Resistor_SMD:R_0402_1005Metric, F.Cu at (207.6, 37.3)
- added R4: 5k1, Resistor_SMD:R_0402_1005Metric, F.Cu at (233.6, 37.3)
- added R5: 10k, Resistor_SMD:R_0402_1005Metric, F.Cu at (240.2, 32.5)
- added R5: 10k, Resistor_SMD:R_0402_1005Metric, F.Cu at (214.2, 32.5)
- added R6: 2k, Resistor_SMD:R_0402_1005Metric, F.Cu at (233.6, 36.3)
- added R6: 2k, Resistor_SMD:R_0402_1005Metric, F.Cu at (207.6, 36.3)
- added R7: 10k, Resistor_SMD:R_0402_1005Metric, F.Cu at (238.8, 32.5)
- added R7: 10k, Resistor_SMD:R_0402_1005Metric, F.Cu at (212.8, 32.5)
- added R8: 10k, Resistor_SMD:R_0402_1005Metric, F.Cu at (209.5, 32.6)
- added R8: 10k, Resistor_SMD:R_0402_1005Metric, F.Cu at (235.5, 32.6)
- added R9: 10k, Resistor_SMD:R_0402_1005Metric, F.Cu at (228.3, 24.4)
- added R9: 10k, Resistor_SMD:R_0402_1005Metric, F.Cu at (202.3, 24.4)
- added U1: USB-C, CustomFootprints:USB-C-SMD_G-SWITCH_GT-USB-7010EN, F.Cu at (205.1, 47.6)
- added U1: USB-C, CustomFootprints:USB-C-SMD_G-SWITCH_GT-USB-7010EN, F.Cu at (231.1, 47.6)
- added U13: ESP32-C6-MINI-1-N4, CustomFootprints:WIFIM-SMD_61P-L16.6-W13.2-P0.80-ESP32-C6-MINI-1-N4, F.Cu at (237.1, 25.7)
- added U13: ESP32-C6-MINI-1-N4, CustomFootprints:WIFIM-SMD_61P-L16.6-W13.2-P0.80-ESP32-C6-MINI-1-N4, F.Cu at (211.1, 25.7)
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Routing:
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- removed copper zone on F.Cu, net Board_2-+3V3
- removed copper zone on F.Cu, net Board_2-GND
- removed copper zone on In1.Cu, net Board_2-GND
- removed copper zone on In2.Cu, net Board_2-GND
- removed copper zone on F.Cu, net Board_2-PWR_VIN
- removed copper zone on F.Cu, net Board_3-+3V3
- removed copper zone on F.Cu, net Board_3-GND
- removed copper zone on In1.Cu, net Board_3-GND
- removed copper zone on In2.Cu, net Board_3-GND
- removed copper zone on F.Cu, net Board_3-PWR_VIN
- removed copper zone on F.Cu, net Board_4-+3V3
- removed copper zone on F.Cu, net Board_4-GND
- removed copper zone on In1.Cu, net Board_4-GND
- removed copper zone on In2.Cu, net Board_4-GND
- removed copper zone on F.Cu, net Board_4-PWR_VIN
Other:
- board size 142 x 116 mm -> 64 x 116 mm
